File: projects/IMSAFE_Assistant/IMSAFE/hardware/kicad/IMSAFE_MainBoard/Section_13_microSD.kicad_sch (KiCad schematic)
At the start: 0 parts

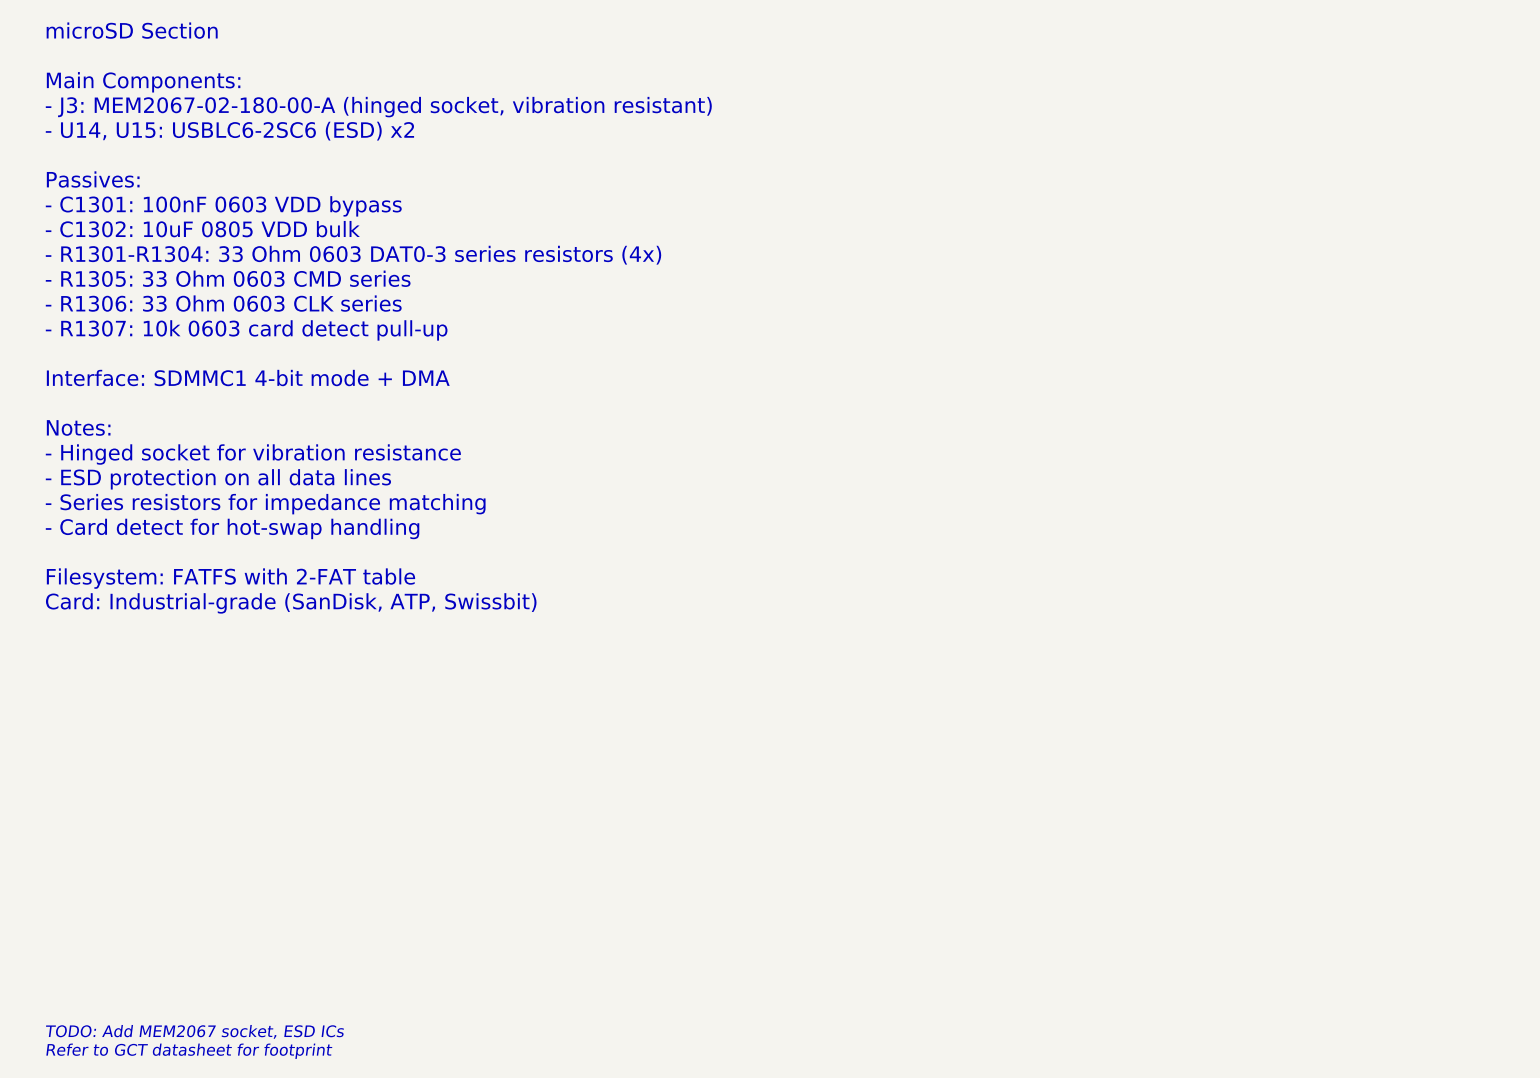
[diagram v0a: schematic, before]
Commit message: Update KiCad schematics and add analysis files
- Update all MainBoard schematic sections with component placement
- Add ERC reports and analysis scripts for schematic validation
- Update Radar Interface and SwitchLED Board projects
- Sync KiCad project files with latest session changes

Co-Authored-By: Claude Opus 4.5 <noreply@anthropic.com>
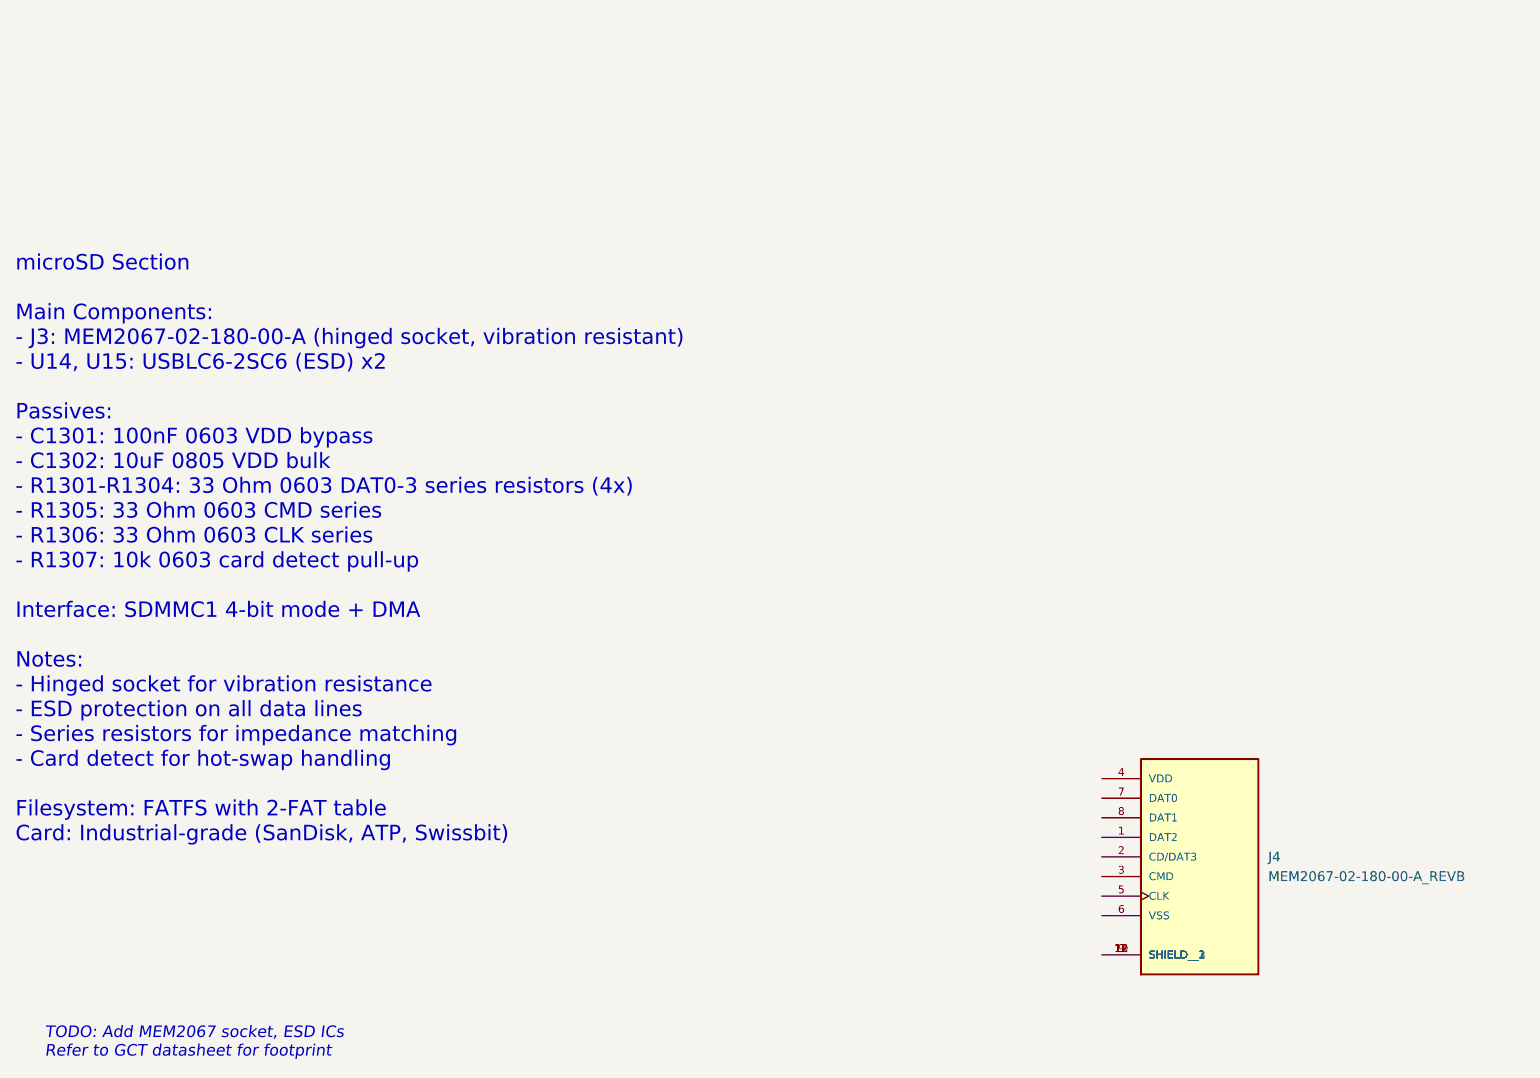
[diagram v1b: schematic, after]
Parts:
- added J4: MEM2067-02-180-00-A_REVB, MEM2067-02-180-00-A_REVB:GCT_MEM2067-02-180-00-A_REVB, symbol 1_New_library:MEM2067-02-180-00-A_REVB
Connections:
- new net: J4.10 (SHIELD__1), J4.11 (SHIELD__2), J4.12 (SHIELD__3), J4.9 (SHIELD)
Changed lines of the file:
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@@
 (kicad_sch
-	(version 20231120)
+	(version 20250114)
 	(generator "eeschema")
-	(generator_version "8.0")
-	(uuid "sec13-0001-0002-0003-000000000001")
+	(generator_version "9.0")
 	(paper "A4")
 	(title_block
@@
 	(text "microSD Section\n\nMain Components:\n- J3: MEM2067-02-180-00-A (hinged socket, vibration resistant)\n- U14, U15: USBLC6-2SC6 (ESD) x2\n\nPassives:\n- C1301: 100nF 0603 VDD bypass\n- C1302: 10uF 0805 VDD bulk\n- R1301-R1304: 33 Ohm 0603 DAT0-3 series resistors (4x)\n- R1305: 33 Ohm 0603 CMD series\n- R1306: 33 Ohm 0603 CLK series\n- R1307: 10k 0603 card detect pull-up\n\nInterface: SDMMC1 4-bit mode + DMA\n\nNotes:\n- Hinged socket for vibration resistance\n- ESD protection on all data lines\n- Series resistors for impedance matching\n- Card detect for hot-swap handling\n\nFilesystem: FATFS with 2-FAT table\nCard: Industrial-grade (SanDisk, ATP, Swissbit)"
 		(exclude_from_sim no)
-		(at 25.4 25.4 0)
+		(at 21.59 55.372 0)
 		(effects
 			(font
@@
 			(justify left)
 		)
-		(uuid "sec13-text-001")
 	)
 	(text "TODO: Add MEM2067 socket, ESD ICs\nRefer to GCT datasheet for footprint"
@@
 			(justify left)
 		)
-		(uuid "sec13-todo-001")
+	)
+	(symbol
+		(lib_id "1_New_library:MEM2067-02-180-00-A_REVB")
+		(at 167.64 95.25 0)
+		(unit 1)
+		(exclude_from_sim no)
+		(in_bom yes)
+		(on_board yes)
+		(dnp no)
+		(fields_autoplaced yes)
+		(property "Reference" "J4"
+			(at 184.15 95.2499 0)
+			(effects
+				(font
+					(size 1.27 1.27)
+				)
+				(justify left)
+			)
+		)
+		(property "Value" "MEM2067-02-180-00-A_REVB"
+			(at 184.15 97.7899 0)
+			(effects
+				(font
+					(size 1.27 1.27)
+				)
+				(justify left)
+			)
+		)
+		(property "Footprint" "MEM2067-02-180-00-A_REVB:GCT_MEM2067-02-180-00-A_REVB"
+			(at 167.64 95.25 0)
+			(effects
+				(font
+					(size 1.27 1.27)
+				)
+				(justify bottom)
+				(hide yes)
+			)
+		)
+		(property "Datasheet" ""
+			(at 167.64 95.25 0)
+			(effects
+				(font
+					(size 1.27 1.27)
+				)
+				(hide yes)
+			)
+		)
+		(property "Description" ""
+			(at 167.64 95.25 0)
+			(effects
+				(font
+					(size 1.27 1.27)
+				)
+				(hide yes)
+			)
+		)
+		(property "MANUFACTURER" "GCT"
+			(at 167.64 95.25 0)
+			(effects
+				(font
+					(size 1.27 1.27)
+				)
+				(justify bottom)
+				(hide yes)
+			)
+		)
+		(pin "5"
+		)
+		(pin "7"
+		)
+		(pin "2"
+		)
+		(pin "8"
+		)
+		(pin "1"
+		)
+		(pin "6"
+		)
+		(pin "12"
+		)
+		(pin "4"
+		)
+		(pin "11"
+		)
+		(pin "3"
+		)
+		(pin "9"
+		)
+		(pin "10"
+		)
+		(instances
+			(project ""
+				(path "/a1b2c3d4-e5f6-7890-abcd-ef1234567890/5fe94529-d5ef-4a5e-bbcf-03b902aeec54"
+					(reference "J4")
+					(unit 1)
+				)
+			)
+		)
 	)
 )
